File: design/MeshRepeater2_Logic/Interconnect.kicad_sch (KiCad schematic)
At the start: 9 parts, among them J11 LC OUT - SYS 3V3, J201 INTERBOARD 2x6 VERTICAL

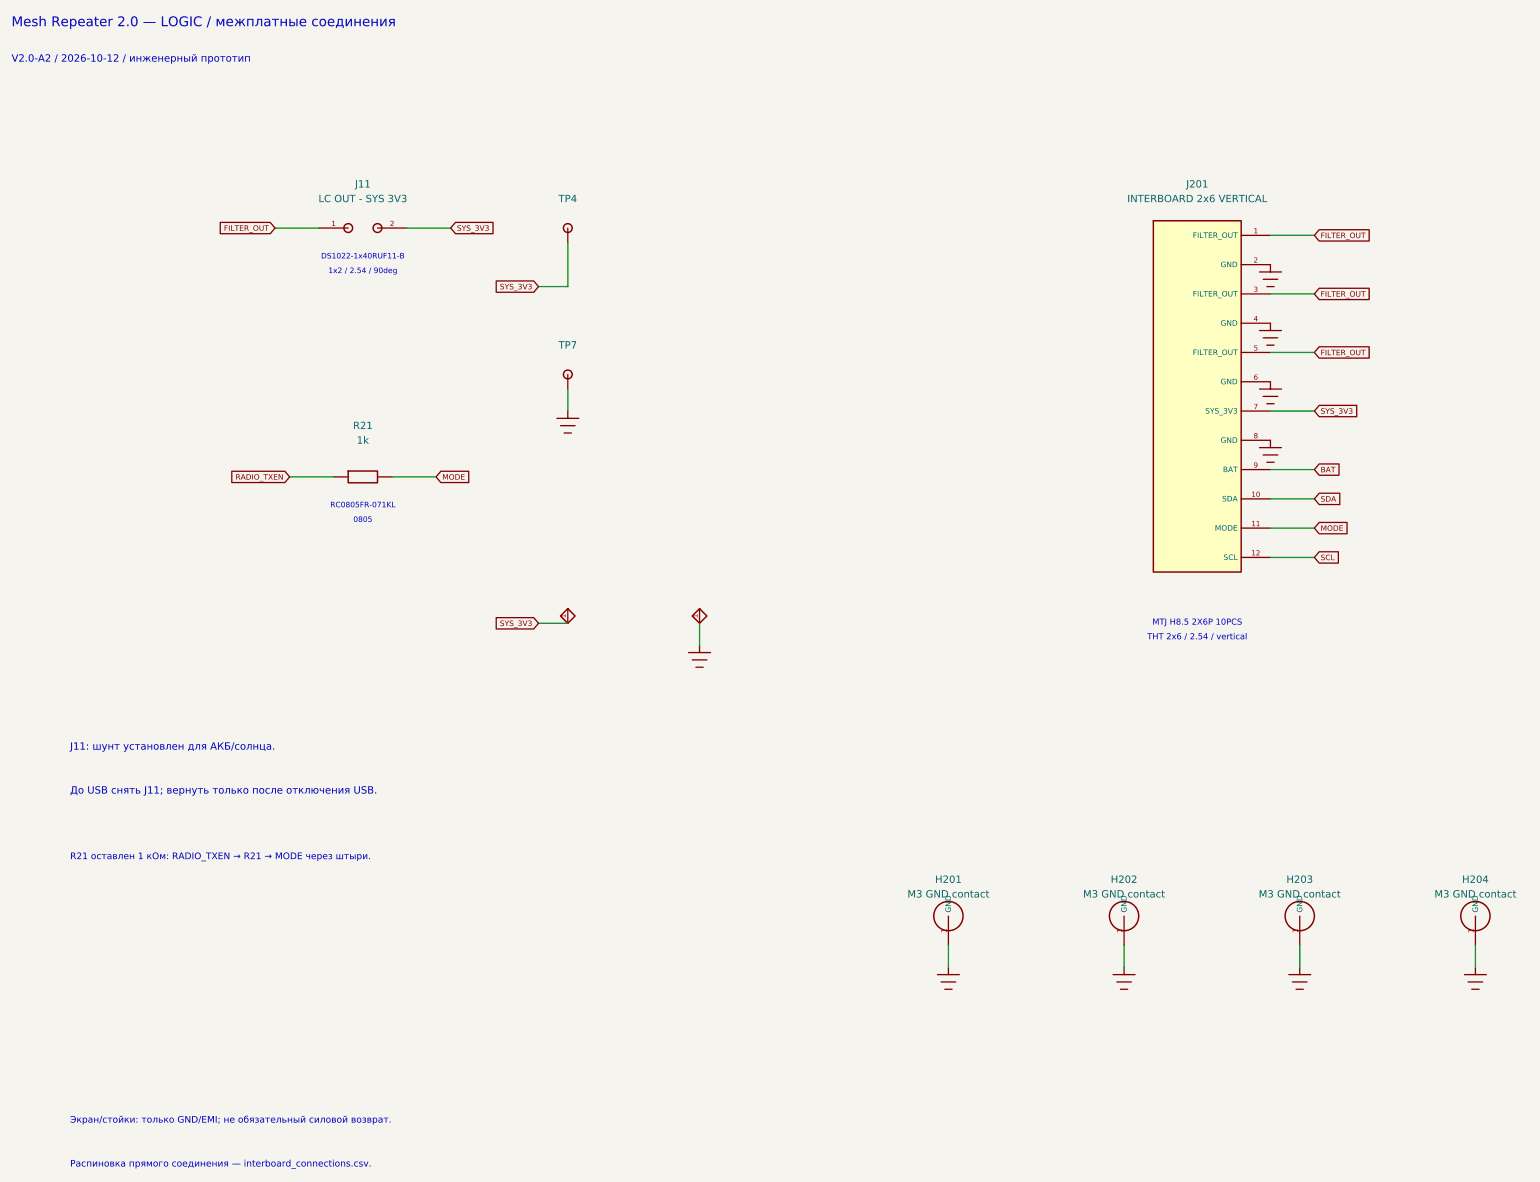
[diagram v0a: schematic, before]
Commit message: Publish Mesh Repeater 2.0 A3 prototype and engineering audit
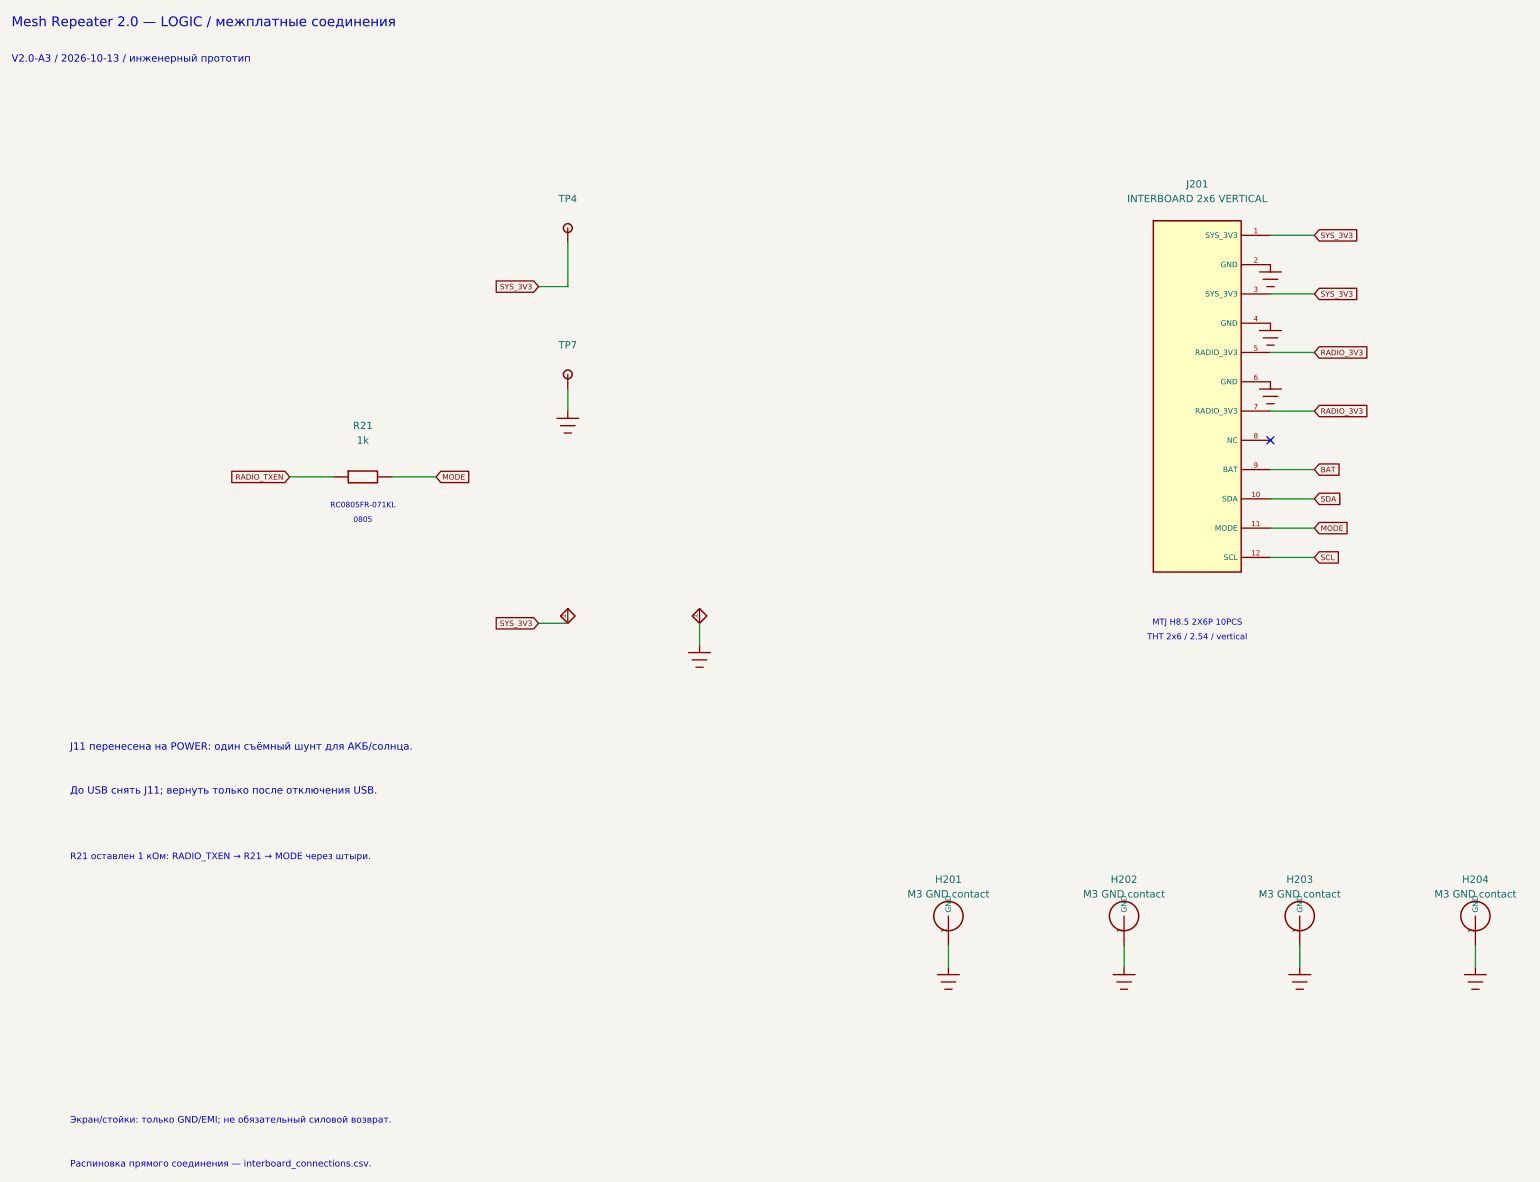
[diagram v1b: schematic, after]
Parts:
- removed J11: LC OUT - SYS 3V3, Meshcore:Connfly_DS1022_1x02RUF11_B_Horizontal__V2_J11, symbol Meshcore:JUMPER_H
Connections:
- net GND: no longer J201.8 (GND)
- net SYS_3V3: now also J201.1 (SYS_3V3), J201.3 (SYS_3V3); no longer J201.7 (SYS_3V3)
- removed net FILTER_OUT: J201.1 (FILTER_OUT), J201.3 (FILTER_OUT), J201.5 (FILTER_OUT)
- new net RADIO_3V3: J201.5 (RADIO_3V3), J201.7 (RADIO_3V3)
- no-connect marks 0 -> 1
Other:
- note added: "J11 перенесена на POWER: один съёмный шунт для АКБ/солнца."
- note added: "V2.0-A3 / 2026-10-13 / инженерный прототип"
- note removed: "1x2 / 2.54 / 90deg"
- note removed: "DS1022-1x40RUF11-B"
- note removed: "J11: шунт установлен для АКБ/солнца."
- note removed: "V2.0-A2 / 2026-10-12 / инженерный прототип"
